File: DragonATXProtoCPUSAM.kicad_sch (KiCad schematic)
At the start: 17 parts, among them IC1 MC6809E, IC2 MC6883, IC3 74LS138, IC4 74LS02

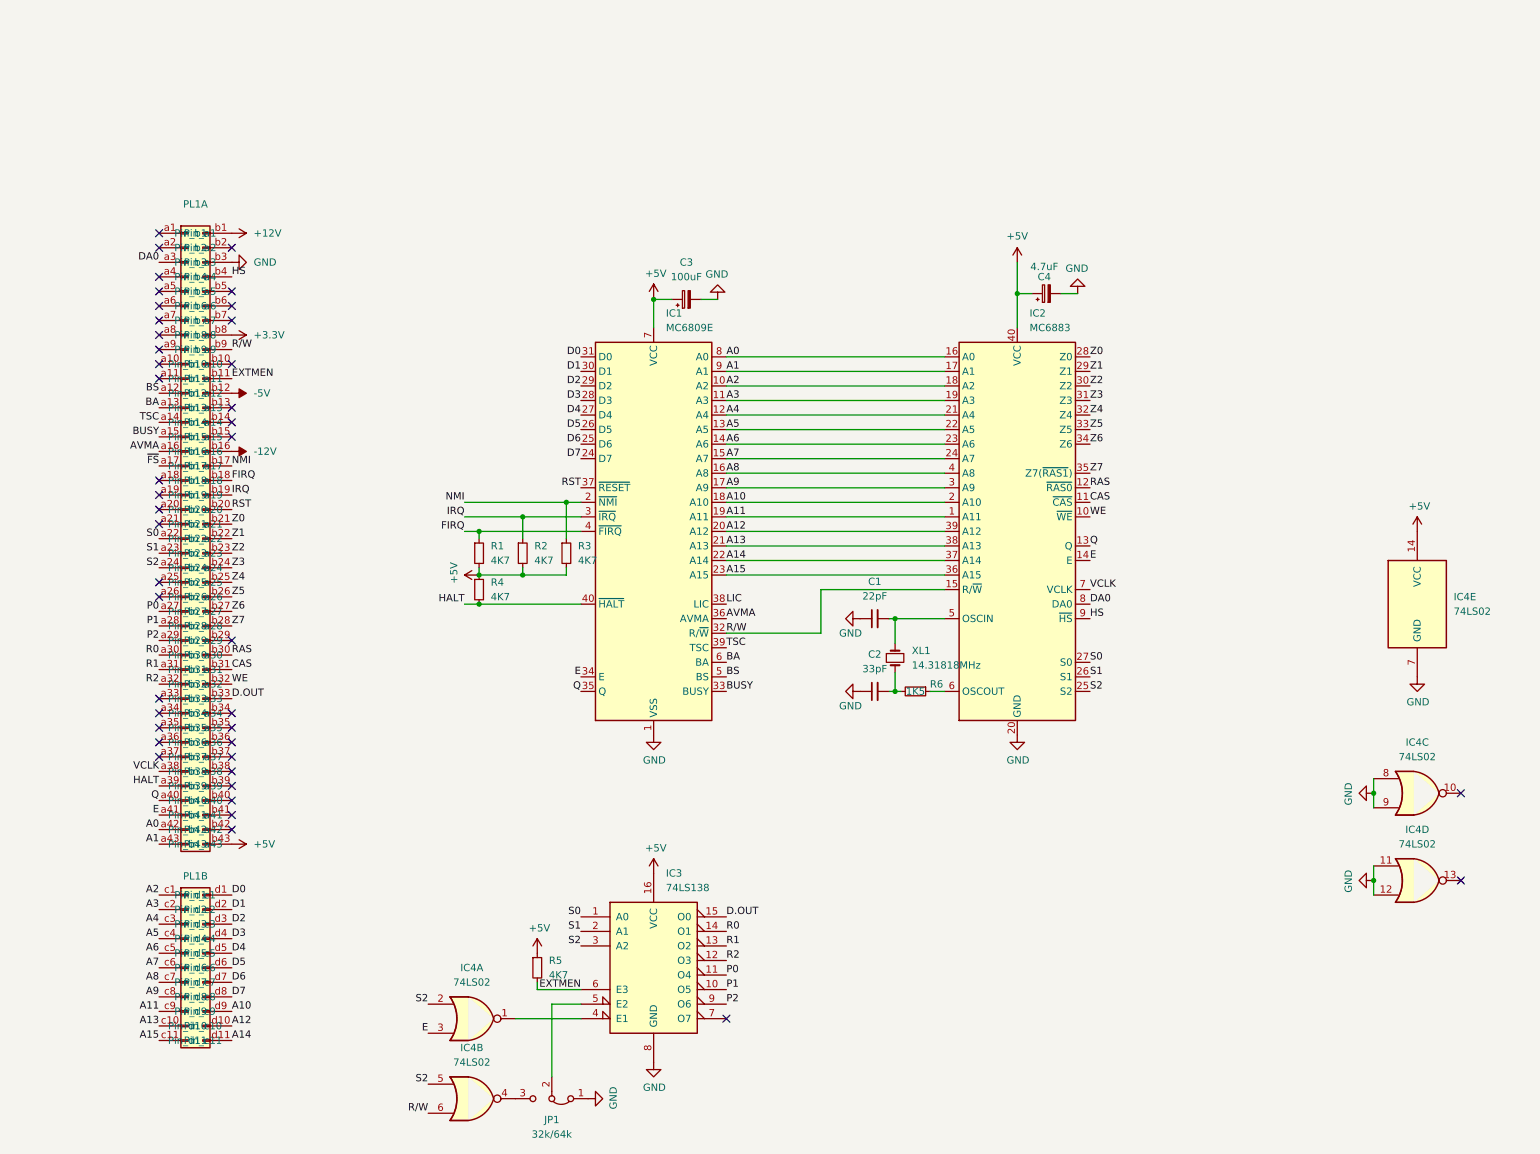
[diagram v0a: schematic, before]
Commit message: add 256K banker
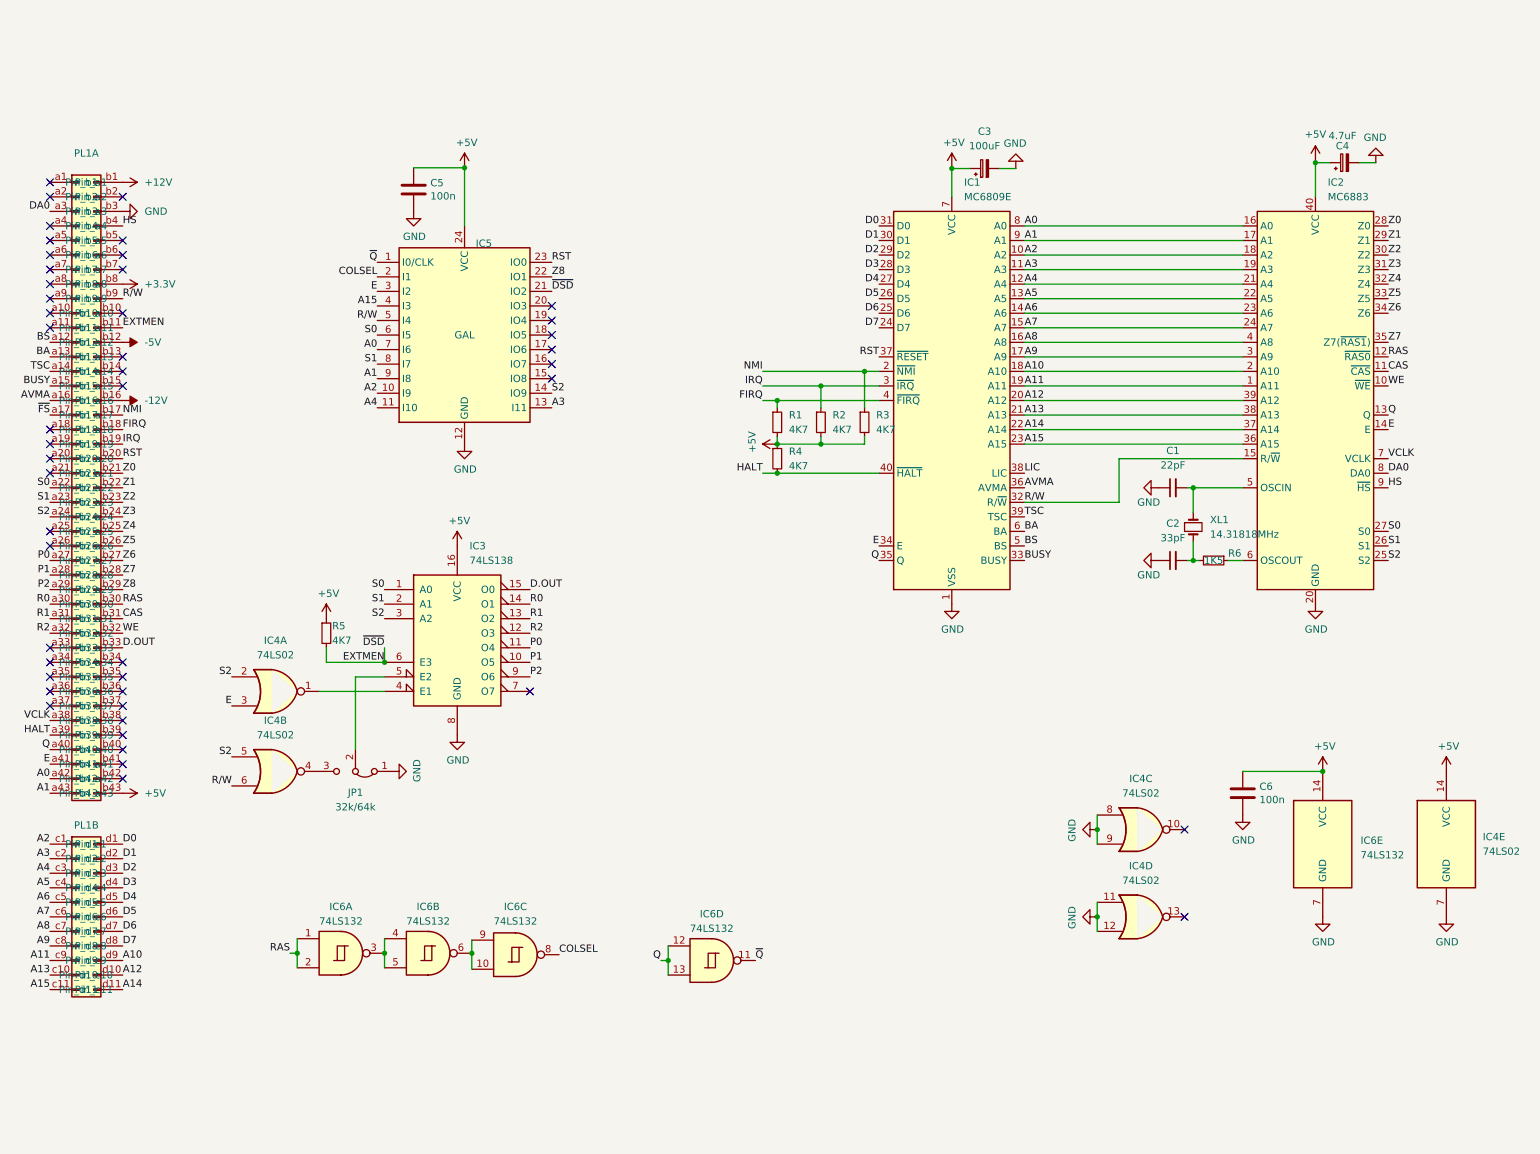
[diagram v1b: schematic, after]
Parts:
- added C5, C6: 100n, Capacitor_THT:C_Rect_L7.0mm_W2.5mm_P5.00mm, symbol Device:C
- added IC5: GAL, Package_DIP:DIP-24_W7.62mm, symbol vdg:GAL22V10
- added IC6: 74LS132, Package_DIP:DIP-14_W7.62mm, symbol 74xx:74LS132
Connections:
- net +5V: now also C5.1, C6.1, IC5.24 (VCC), IC6.14 (VCC)
- net A0: now also IC5.7 (I6)
- net A1: now also IC5.9 (I8)
- net A15: now also IC5.4 (I3)
- net A2: now also IC5.10 (I9)
- net A3: now also IC5.13 (I11)
- net A4: now also IC5.11 (I10)
- net E: now also IC5.3 (I2)
- net EXTMEN: now also IC5.21 (IO2)
- net GND: now also C5.2, C6.2, IC5.12 (GND), IC6.7 (GND)
- net Q: now also IC6.12, IC6.13
- net RAS: now also IC6.1, IC6.2
- net RST: now also IC5.23 (IO0)
- net R/W: now also IC5.5 (I4)
- net S0: now also IC5.6 (I5)
- net S1: now also IC5.8 (I7)
- net S2: now also IC5.14 (IO9)
- net Z8: now reaches PL1.b29 (Pin_b29)
- net Z8: now also IC5.22 (IO1)
- new net: IC6.3, IC6.4, IC6.5
- new net: IC6.10, IC6.6, IC6.9
- new net COLSEL: IC5.2 (I1), IC6.8
- new net ~{Q}: IC5.1 (I0/CLK), IC6.11
- no-connect marks 42 -> 47
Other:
- moved on the sheet: C1, C2, C3, C4, IC1, IC2, IC3, IC4A, IC4B, IC4C, IC4D, IC4E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

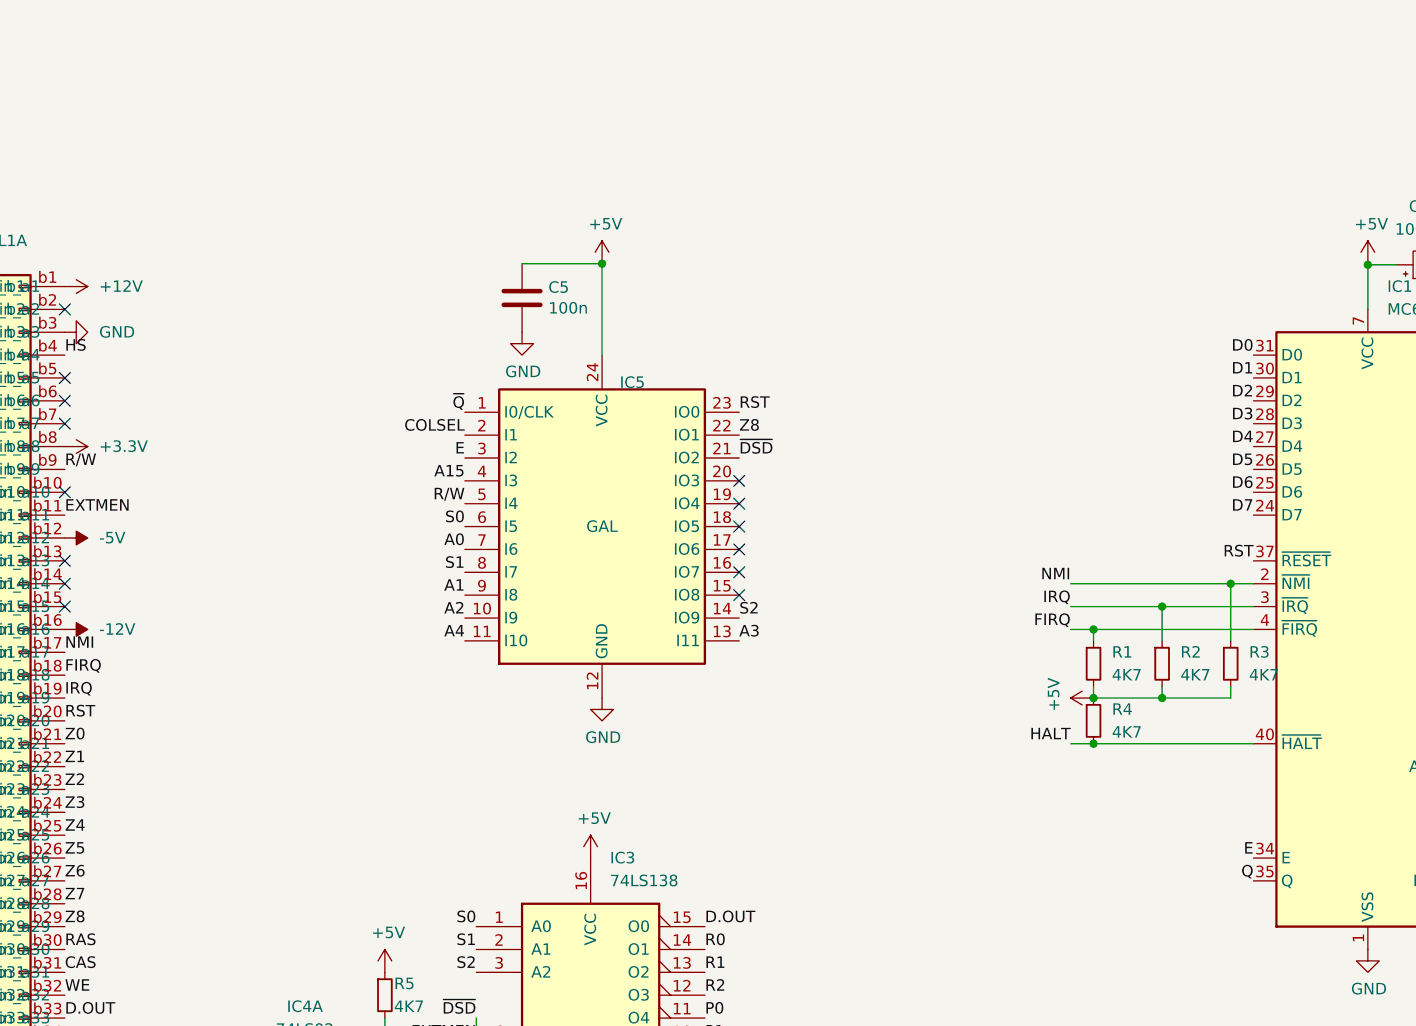
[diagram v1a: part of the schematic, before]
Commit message: Include pull-up/down on data lines to allow quick forcing on selected inputs (for NOP)
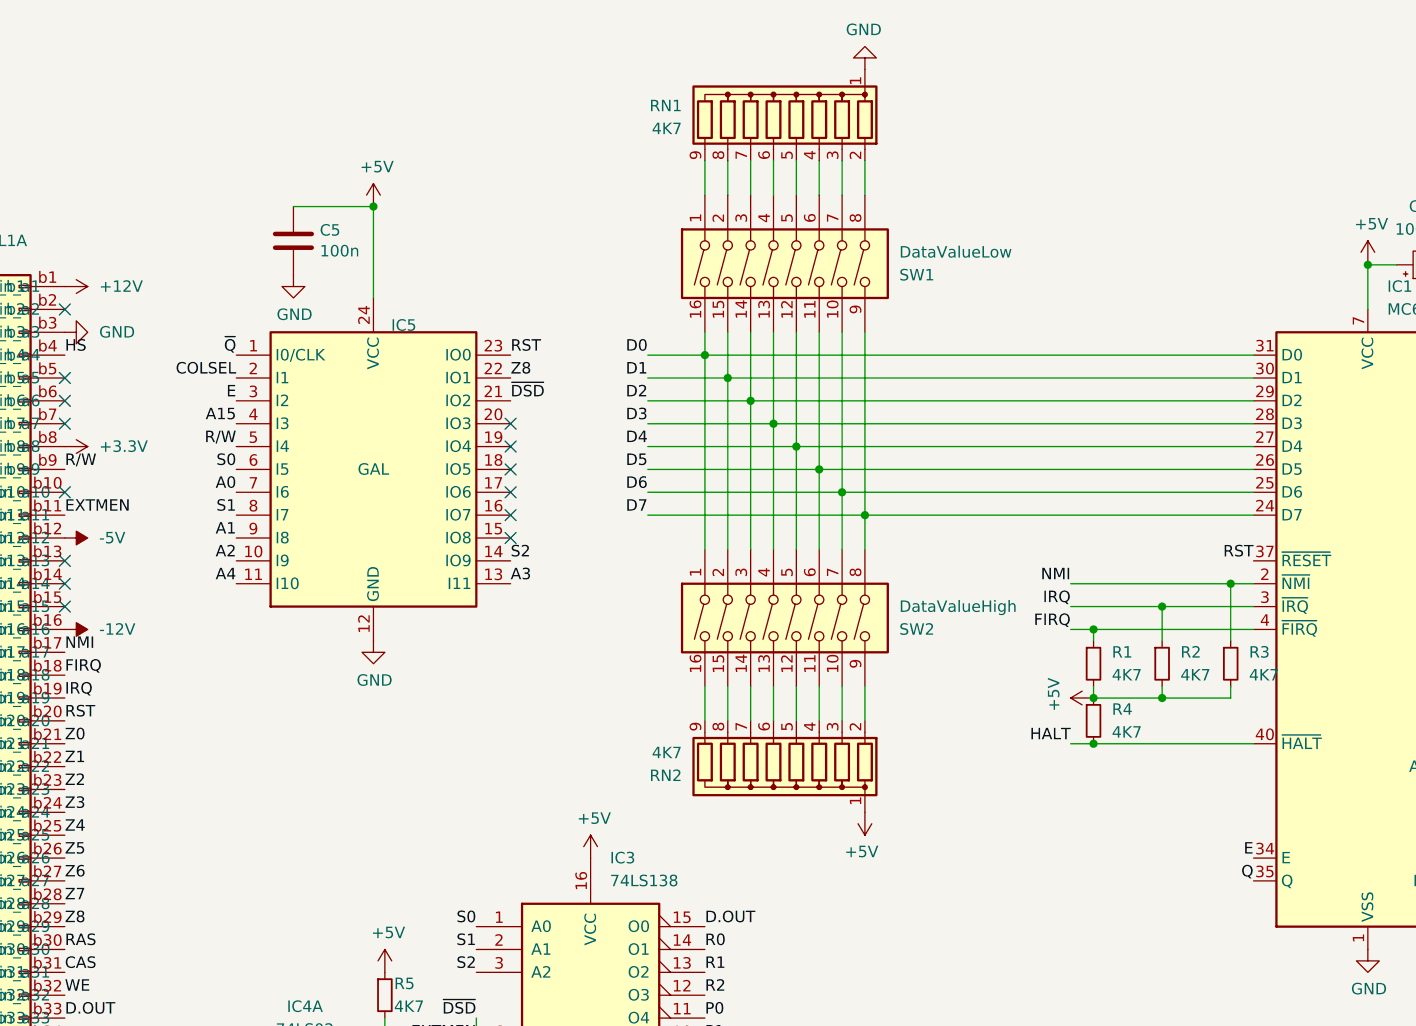
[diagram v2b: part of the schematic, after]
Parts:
- added RN1, RN2: 4K7, Resistor_THT:R_Array_SIP9, symbol Device:R_Network08
- added SW1: DataValueLow, Package_DIP:DIP-16_W7.62mm, symbol Switch:SW_DIP_x08
- added SW2: DataValueHigh, Package_DIP:DIP-16_W7.62mm, symbol Switch:SW_DIP_x08
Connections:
- net +5V: now also RN2.1 (common)
- net D0: now also SW1.16, SW2.1
- net D1: now also SW1.15, SW2.2
- net D2: now also SW1.14, SW2.3
- net D3: now also SW1.13, SW2.4
- net D4: now also SW1.12, SW2.5
- net D5: now also SW1.11, SW2.6
- net D6: now also SW1.10, SW2.7
- net D7: now also SW1.9, SW2.8
- net GND: now also RN1.1 (common)
- new net: RN2.3 (R2), SW2.10
- new net: RN2.4 (R3), SW2.11
- new net: RN2.5 (R4), SW2.12
- new net: RN2.6 (R5), SW2.13
- new net: RN2.7 (R6), SW2.14
- new net: RN2.8 (R7), SW2.15
- new net: RN2.9 (R8), SW2.16
- new net: RN2.2 (R1), SW2.9
- new net: RN1.9 (R8), SW1.1
- new net: RN1.8 (R7), SW1.2
- new net: RN1.7 (R6), SW1.3
- new net: RN1.6 (R5), SW1.4
- new net: RN1.5 (R4), SW1.5
- new net: RN1.4 (R3), SW1.6
- new net: RN1.3 (R2), SW1.7
- new net: RN1.2 (R1), SW1.8
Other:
- moved on the sheet: C5, IC5
